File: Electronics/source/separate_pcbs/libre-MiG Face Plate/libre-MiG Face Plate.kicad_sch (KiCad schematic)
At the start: 7 parts, among them J17 Conn_01x06, J18 Conn_01x03, SW18 SKRHABE010, SW2 SW_Push, SW3 SW_Push

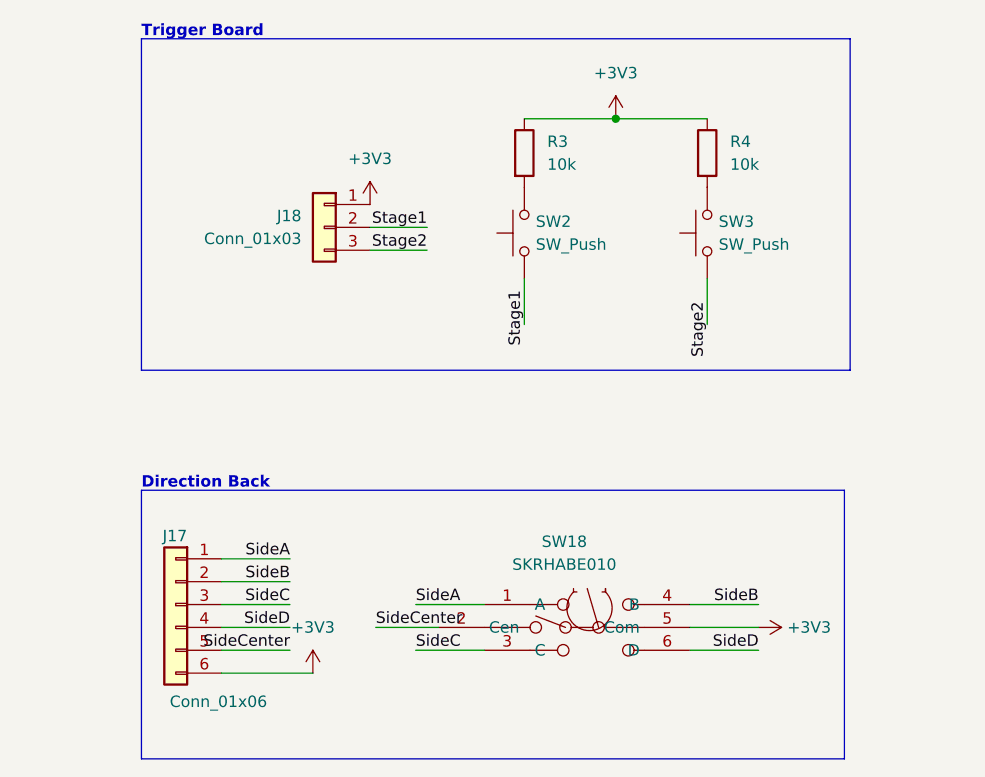
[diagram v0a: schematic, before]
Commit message: started layout and finished board shapes
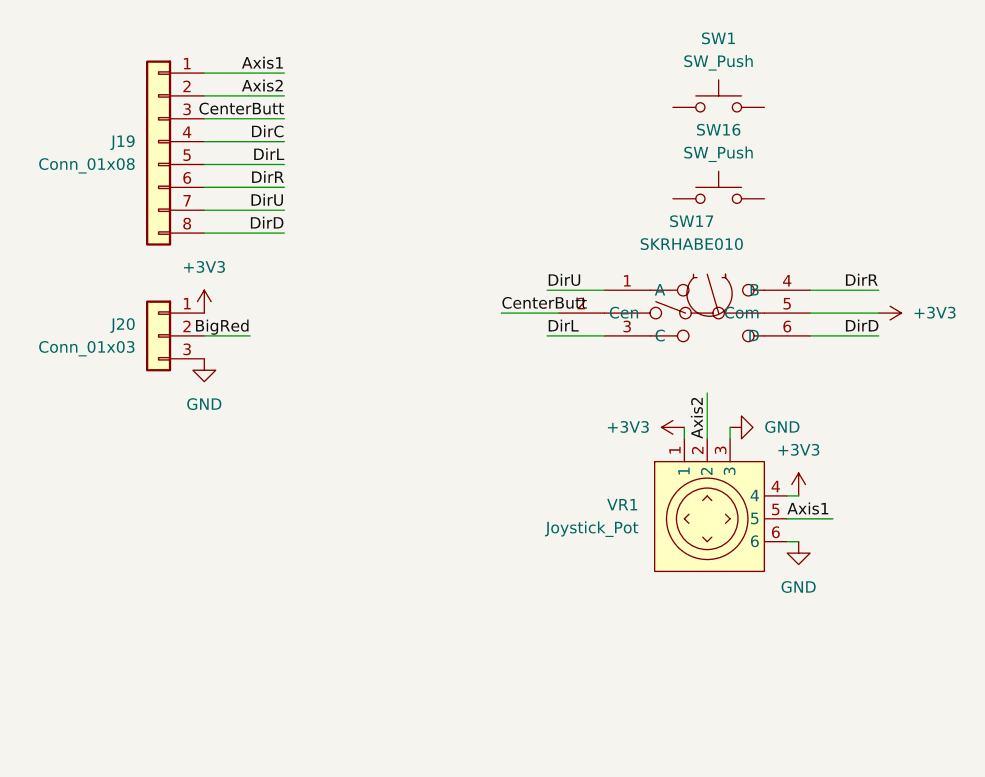
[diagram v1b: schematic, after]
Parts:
- removed J17: Conn_01x06, Connector_JST:JST_PH_S6B-PH-K_1x06_P2.00mm_Horizontal, symbol Connector_Generic:Conn_01x06
- removed J18: Conn_01x03, Connector_JST:JST_PH_S3B-PH-K_1x03_P2.00mm_Horizontal, symbol Connector_Generic:Conn_01x03
- removed R3, R4: 10k, Resistor_SMD:R_0805_2012Metric, symbol Device:R
- removed SW18: SKRHABE010, Personal:SKRHABE010, symbol Personal:SKRHABE010
- removed SW2, SW3: SW_Push, Button_Switch_THT:SW_PUSH-12mm_Wuerth-430476085716, symbol Switch:SW_Push
- added J19: Conn_01x08, Connector_JST:JST_PH_S8B-PH-K_1x08_P2.00mm_Horizontal, symbol Connector_Generic:Conn_01x08
- added J20: Conn_01x03, Connector_JST:JST_PH_B3B-PH-K_1x03_P2.00mm_Vertical, symbol Connector_Generic:Conn_01x03
- added SW1: SW_Push, Button_Switch_THT:SW_PUSH-12mm_Wuerth-430476085716, symbol Switch:SW_Push
- added SW16: SW_Push, Personal:PS1024AL, symbol Switch:SW_Push
- added SW17: SKRHABE010, Personal:SKRHABE010, symbol Personal:SKRHABE010
- added VR1: Joystick_Pot, Personal:RKJXV1220, symbol Personal:Joystick_Pot
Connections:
- net +3V3: now also J20.1 (Pin_1), SW17.5 (Com), VR1.1, VR1.4
- new net Axis1: J19.1 (Pin_1), VR1.5
- new net Axis2: J19.2 (Pin_2), VR1.2
- new net BigRed: J20.2 (Pin_2)
- new net CenterButt: J19.3 (Pin_3), SW17.2 (Cen)
- new net DirC: J19.4 (Pin_4)
- new net DirD: J19.8 (Pin_8), SW17.6 (D)
- new net DirL: J19.5 (Pin_5), SW17.3 (C)
- new net DirR: J19.6 (Pin_6), SW17.4 (B)
- new net DirU: J19.7 (Pin_7), SW17.1 (A)
- new net GND: J20.3 (Pin_3), VR1.3, VR1.6
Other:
- note removed: "Direction Back"
- note removed: "Trigger Board"
- title: Trigger -> Face Plate
